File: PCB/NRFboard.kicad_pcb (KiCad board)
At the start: 6 copper layers, 25.8 x 51.2 mm, 46 parts, among them J1 USB_C_Receptacle_USB2.0_14P, J2 Conn_01x20, J3 Conn_01x20, J4 Conn_01x03, J5 Conn_01x03, SW1 SW_Push, U2 MCP1700x-300xxTT, U4 nRF52840, U7 BQ24075RGT, Y1 32Mhz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

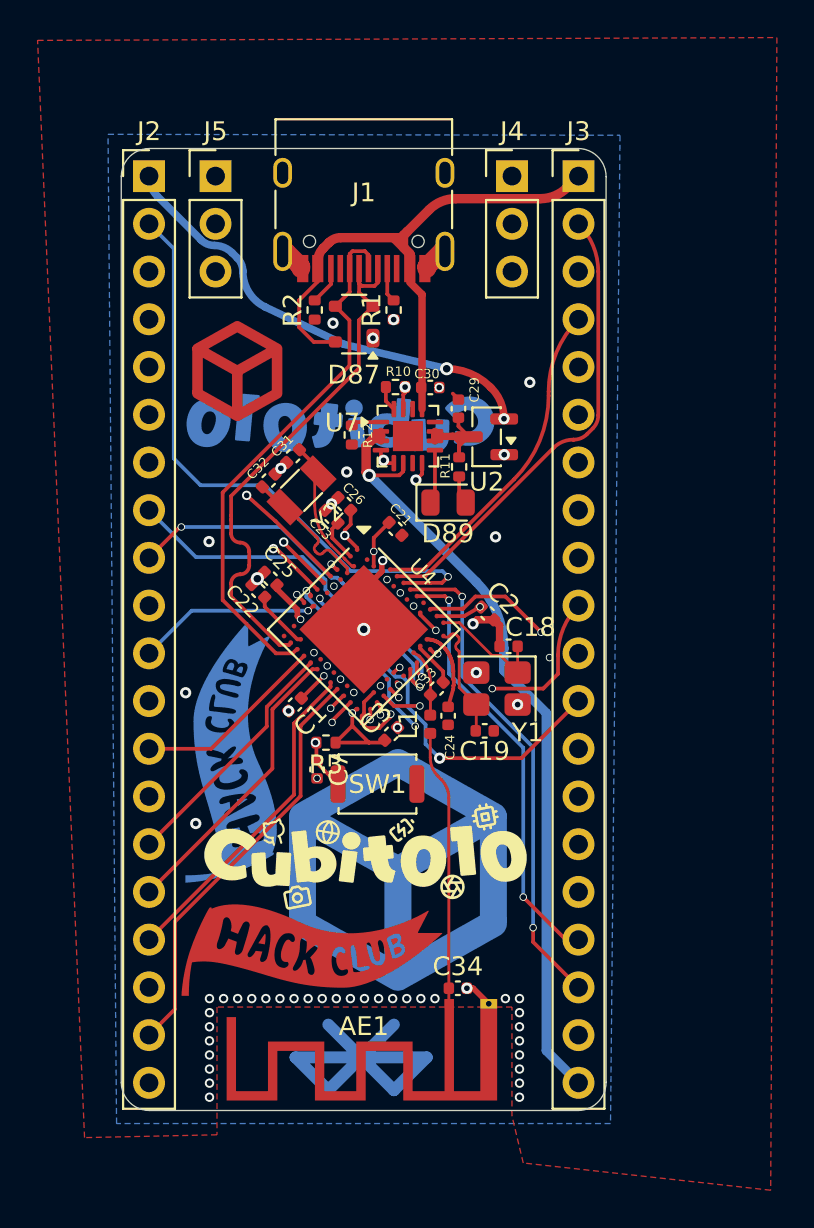
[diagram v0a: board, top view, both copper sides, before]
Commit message: updated routing, should be finalized and ready for production
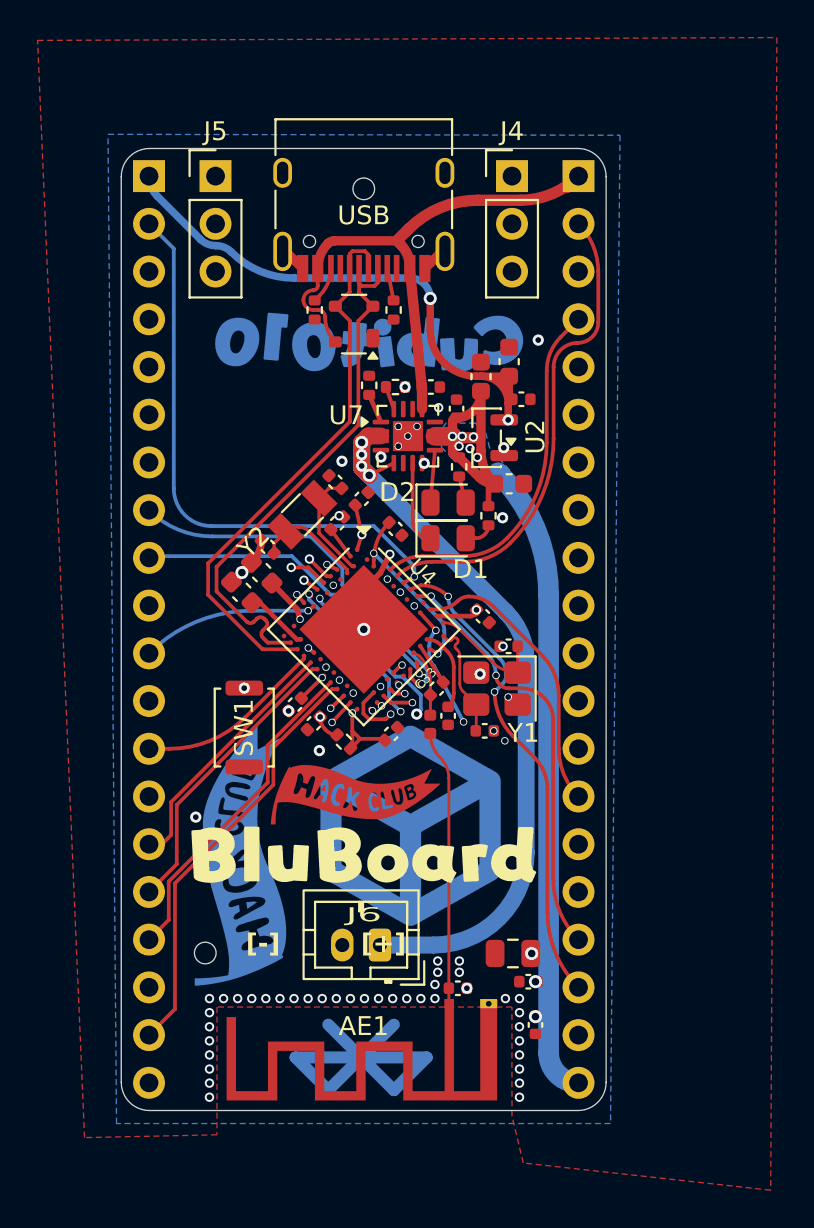
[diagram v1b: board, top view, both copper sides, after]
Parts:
- removed cubit010: cubit010large, Library:cubit010large
- removed hackFront: hack, Library:hack
- removed logo: logo, Library:Untitled
- removed logoCUlarge: logoCUlarge, Library:logoCUlarge
- removed logoSmall: logoCUsmall, Library:logoCUsmall
- added C10: 10uF, Capacitor_SMD:C_0603_1608Metric, F.Cu at (81.2, 94.1)
- added C11: 1uF, Capacitor_SMD:C_0402_1005Metric, F.Cu at (81.8, 89.6)
- added C4: 0.1uF, Capacitor_SMD:C_0402_1005Metric, F.Cu at (82.6, 122.9)
- added C5: 1uF, Capacitor_SMD:C_0402_1005Metric, F.Cu at (82.2, 120.6)
- added C6: 22uF, Capacitor_SMD:C_0805_2012Metric, F.Cu at (81.4, 119.1)
- added C8: 0.1uF, Capacitor_SMD:C_0402_1005Metric, F.Cu at (78.4, 90.1)
- added C9: 10uF, Capacitor_SMD:C_0603_1608Metric, F.Cu at (81.2, 87.6)
- added D1: green, LED_SMD:LED_0805_2012Metric, F.Cu at (78.0, 97.0)
- added J6: Conn_01x02, Connector_JST:JST_PH_B2B-PH-K_1x02_P2.00mm_Vertical, F.Cu at (74.3, 118.7)
- added R4: 1.5k, Resistor_SMD:R_0402_1005Metric, F.Cu at (80.1, 95.8)
- added ToolHole1: ToolingHole_1.152mm, MountingHole:ToolingHole_1.152mm, B.Cu at (73.5, 78.4)
- added ToolHole2: ToolingHole_1.152mm, MountingHole:ToolingHole_1.152mm, F.Cu at (65.0, 119.1)
- added car: car, car:carbig, B.Cu at (68.5, 92.2)
- added cubit010lg: cubit010large, Library:cubit010large, B.Cu at (73.8, 86.5)
- added hacksm: hackSmall, Library:hackSmall, F.Cu at (73.0, 110.7)
- added logobig: logo, Library:logoCU, B.Cu at (76.0, 112.3)
- added logomid: logoCUmid, Library:logoCUmid, F.Cu at (67.6, 89.3)
- C18, C19: value 20pF -> 12pF
- C22, C25, C29: footprint Capacitor_SMD:C_0402_1005Metric -> Capacitor_SMD:C_0603_1608Metric
- C31, C32: value 15pF -> 12.5pF
- J2, J3: moved to B.Cu
- R11: value 10k -> 1.5k
- moved SW1 7.70 mm to (67.1, 107.1), turned to -90 degrees
- moved hackBack 5.51 mm to (66.9, 113.9)
- moved C32 3.53 mm to (68.3, 97.5), turned to 135 degrees
- moved R12 2.80 mm to (73.8, 88.9), turned to 90 degrees
- moved C31 2.64 mm to (72.0, 94.0), turned to 135 degrees
- moved C7 2.46 mm to (70.8, 106.8), turned to -135 degrees
- moved C29 2.08 mm to (79.7, 88.4)
- moved Y2 1.30 mm to (70.2, 95.8)
- moved C26 0.97 mm to (73.3, 94.9), turned to 45 degrees
- moved R3 0.95 mm to (72.4, 107.8), turned to 135 degrees
- moved C22 0.89 mm to (67.0, 99.9)
- moved C25 0.57 mm to (68.0, 98.8)
- moved C23 0.46 mm to (72.0, 96.2), turned to -135 degrees
- moved C2 0.29 mm to (79.8, 101.2)
- moved U2 0.05 mm to (80.0, 91.7)
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- renumbered D89 to D2, J1 to USB
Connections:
- J3 pad 20: VBAT -> Out
- U7 pad 5: GND -> VBAT
- U7 pad 6: VBAT -> GND
- U7 pad 7: unconnected-(U7-~{PGOOD}-Pad7) -> Net-(D1-K)
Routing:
- net Out: track 6.14 -> 50.3 mm, vias 0 -> 9
- net GND: track 17.9 -> 8.77 mm, vias 59 -> 62
- net VBAT: track 42.3 -> 48.0 mm, vias 1 -> 4
- net Net-(D1-K): track 0.00 -> 4.50 mm
- net reset: track 36.8 -> 40.4 mm, vias 2 -> 3
- net +3V3: track 76.6 -> 79.9 mm
- net 111: track 18.3 -> 15.7 mm
- net AIN0/002: track 32.7 -> 30.6 mm
- net NFC2/010: track 19.8 -> 17.7 mm, vias 2 -> 1
- net VBUS: track 33.1 -> 31.0 mm
- net 106: track 13.1 -> 15.0 mm
- net Net-(U4-XL1/P0.00): track 7.46 -> 5.87 mm
- net Net-(U4-XL2/P0.01): track 7.44 -> 5.86 mm
- net Net-(D1-A): track 0.00 -> 1.58 mm
- net AIN7/031: track 18.0 -> 19.4 mm
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- added copper zone on F.Cu, net +3V3
- added copper zone on In2.Cu, net +3V3
- added copper zone on B.Cu, net Out
- added copper zone on F.Cu, net Out
- added copper zone on In1.Cu, net Out
- added copper zone on In2.Cu, net Out
- added copper zone on In3.Cu, net Out
- added copper zone on In4.Cu, net Out
- added copper zone on In4.Cu, net reset
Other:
- board text added: "[-] [+]"

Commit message: update rf, wanted to add qspi but reverted
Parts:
- removed blutooth: blutoo, Library:blutoo
- added R5: 1.2k, Resistor_SMD:R_0402_1005Metric, F.Cu at (77.5, 88.8)
- added rstcont1: TestPoint, TestPoint:TestPoint_Pad_D1.0mm, B.Cu at (79.3, 77.7)
- C18, C19: value 12pF -> 20pF
- C31, C32: value 12.5pF -> 22pF
- R10: value 2K -> 1.1k
- moved C30 0.95 mm to (76.1, 89.0), turned to 180 degrees
- moved R10 0.64 mm to (74.7, 88.5), turned to -90 degrees
- moved logobig 0.49 mm to (75.7, 111.9)
- moved hacksm 0.37 mm to (73.0, 111.0)
- moved SW1 0.20 mm to (67.3, 107.1), turned to -45 degrees
- renumbered USB to J1
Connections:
- net Net-(D1-A) renamed /green
- net Net-(D2-A) renamed /orange
- U7 pad 12: unconnected-(U7-ILIM-Pad12) -> Net-(U7-ILIM)
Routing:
- net Net-(U7-ILIM): track 0.00 -> 1.47 mm
- net reset: track 40.4 -> 41.7 mm
- net AIN5/029: track 25.6 -> 24.4 mm, vias 0 -> 1
- net +3V3: track 79.9 -> 78.8 mm
- net GND: track 8.77 -> 9.49 mm, vias 62 -> 132
- net 022: track 22.7 -> 23.4 mm
- net 020: track 17.7 -> 18.4 mm
- net AIN6/030: track 20.5 -> 19.9 mm
- net 115: track 25.7 -> 26.2 mm
- net Out: track 50.3 -> 49.8 mm

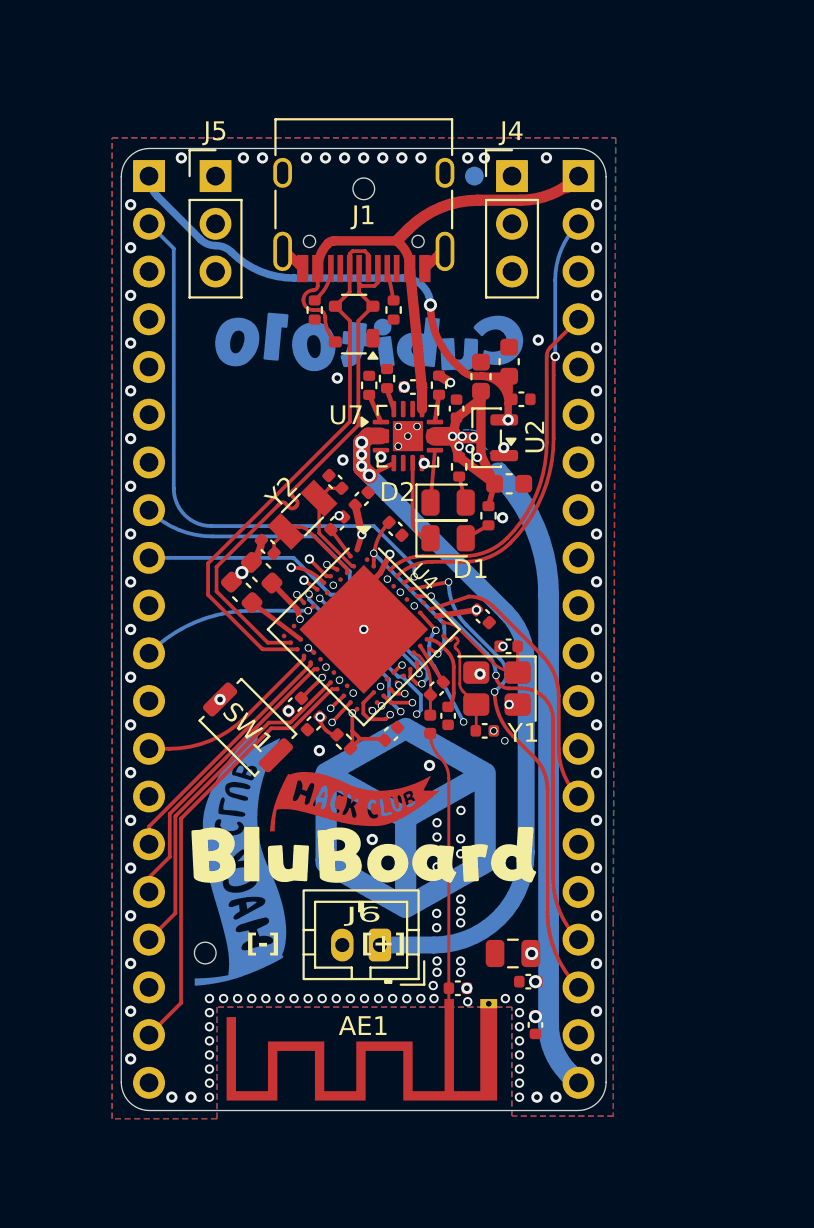
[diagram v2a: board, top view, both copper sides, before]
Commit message: updated layout, added more vias, matched impedance for usb line for a coplanar diff
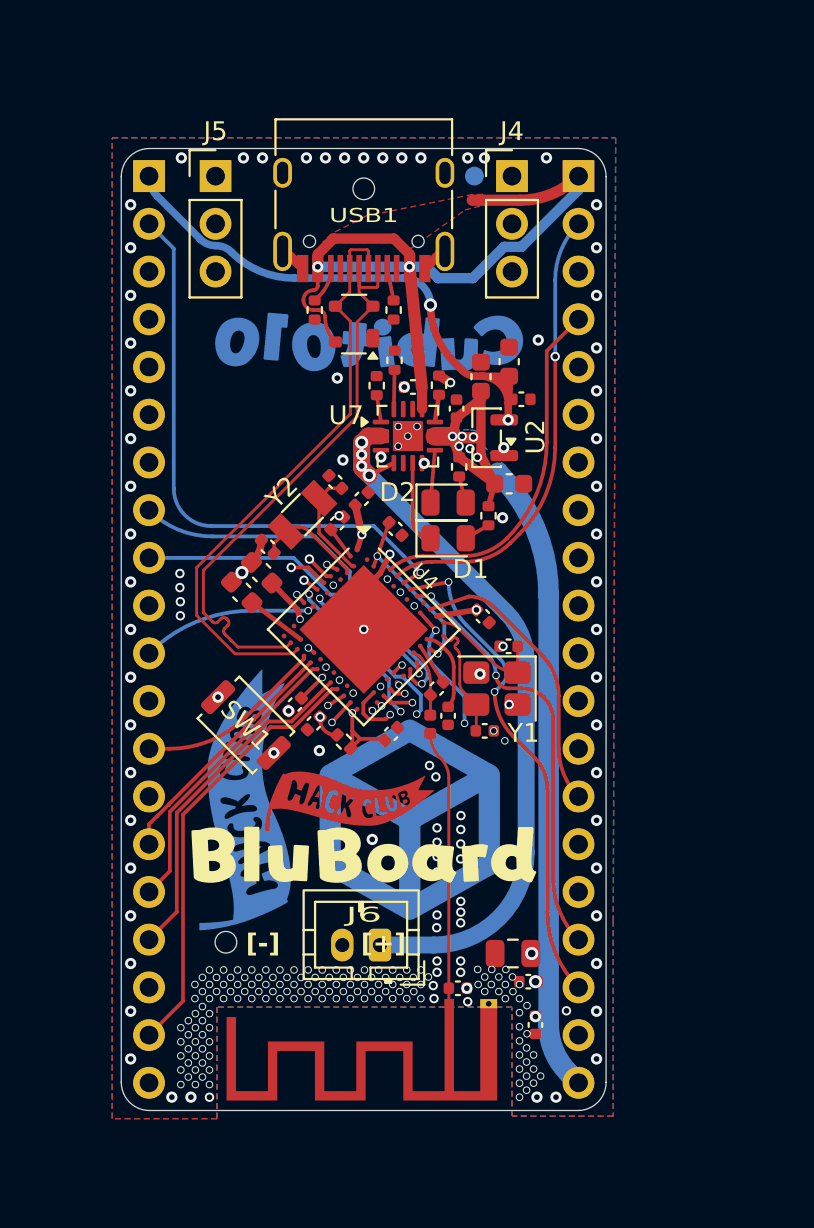
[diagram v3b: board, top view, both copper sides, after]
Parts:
- moved hackBack 2.96 mm to (67.2, 110.9)
- moved ToolHole2 1.24 mm to (66.1, 118.5)
- moved R10 1.05 mm to (75.1, 87.5)
- moved logomid 0.47 mm to (67.5, 88.8)
- moved R12 0.40 mm to (74.2, 88.9)
- moved hacksm 0.28 mm to (72.7, 111.0)
- moved logobig 0.24 mm to (75.9, 112.0)
- moved SW1 0.17 mm to (67.2, 106.9)
- renumbered AE1 to BLE1, J1 to USB1
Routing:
- net VBUS: track 31.0 -> 42.4 mm, vias 0 -> 2
- net USB_D-: track 29.7 -> 31.7 mm
- net USB_D+: track 29.7 -> 31.8 mm
- net 108: track 18.8 -> 17.7 mm
- net 112: track 21.8 -> 22.6 mm
- net Net-(U7-ISET): track 1.25 -> 2.09 mm
- net AIN6/030: track 19.9 -> 20.5 mm
- net GND: vias 132 -> 252
- added copper zone on F.Cu, net VBUS
